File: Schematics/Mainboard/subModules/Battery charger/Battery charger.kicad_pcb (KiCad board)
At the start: 2 copper layers, 20.1 x 20.1 mm, 15 parts, among them J1 Input, J2 Output, U1 BQ25300

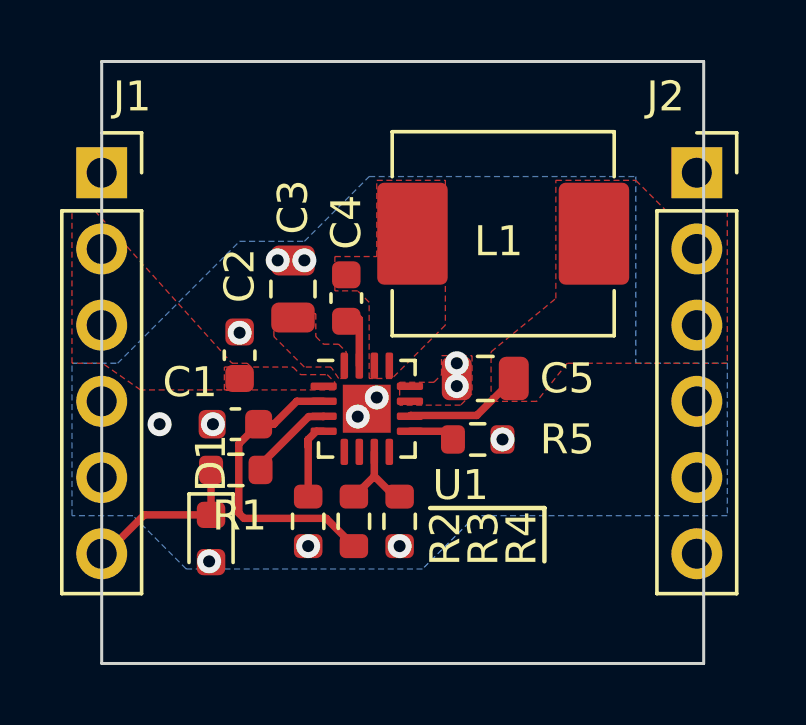
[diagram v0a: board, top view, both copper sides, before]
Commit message: Added gerbers for batt charger
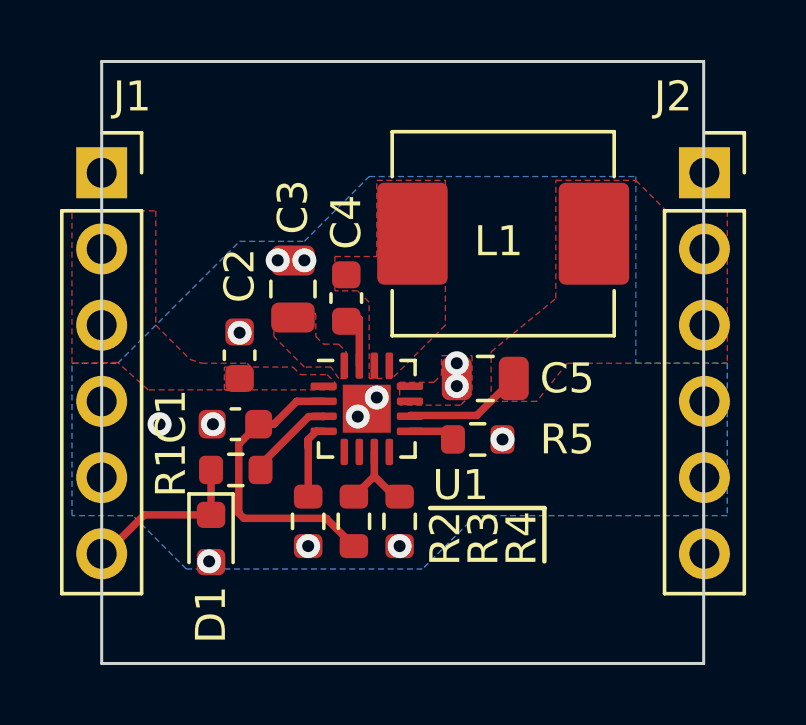
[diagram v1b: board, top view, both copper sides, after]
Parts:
- moved J2 0.25 mm to (113.3, 59.7)
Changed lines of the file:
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@@
     (property "Sheetname" "")
     (attr smd)
-    (fp_text reference "D1" (at -2.5145 0 90) (layer "F.SilkS")
+    (fp_text reference "D1" (at 2.54 0 90) (layer "F.SilkS")
       (effects (font (size 1 1) (thickness 0.15)))
     )
@@
   )
   (footprint "Connector_PinSocket_2.54mm:PinSocket_1x06_P2.54mm_Vertical" (layer "F.Cu")
-    (at 113.03 59.69)
+    (at 113.284 59.69)
     (descr "Through hole straight socket strip, 1x06, 2.54mm pitch, single row (from Kicad 4.0.7), script generated")
     (tags "Through hole socket strip THT 1x06 2.54mm single row")
@@
     (property "Sheetname" "")
     (attr smd)
-    (fp_text reference "R1" (at 0.127 1.524) (layer "F.SilkS")
+    (fp_text reference "R1" (at -2.159 0 90) (layer "F.SilkS")
       (effects (font (size 1 1) (thickness 0.15)))
     )
@@
     (property "Sheetname" "")
     (attr smd)
-    (fp_text reference "C1" (at -1.511 -1.397) (layer "F.SilkS")
+    (fp_text reference "C1" (at -2.146 -0.254 90) (layer "F.SilkS")
       (effects (font (size 1 1) (thickness 0.15)))
     )
@@
     (polygon
       (pts
-        (xy 97.536 66.04)
+        (xy 94.996 64.77)
+        (xy 96.139 65.913)
+        (xy 96.52 66.04)
         (xy 98.044 66.04)
         (xy 98.171 66.167)
         (xy 98.171 66.929)
-        (xy 94.488 66.929)
-        (xy 93.218 66.04)
+        (xy 94.742 66.929)
+        (xy 93.726 66.015)
         (xy 92.202 66.04)
         (xy 92.202 60.96)
-        (xy 92.964 60.96)
+        (xy 94.996 60.96)
       )
     )
